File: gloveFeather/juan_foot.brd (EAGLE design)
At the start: 44.4 x 59.4 mm, 8 parts

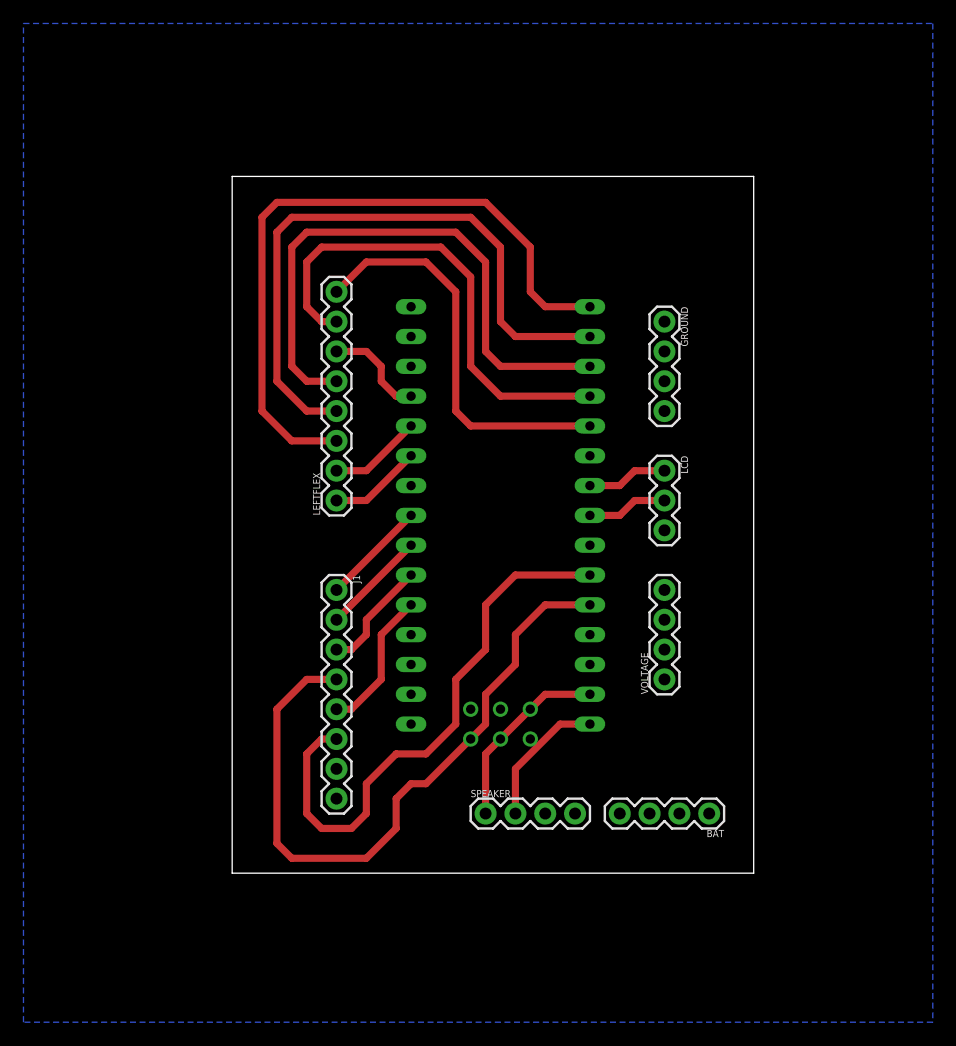
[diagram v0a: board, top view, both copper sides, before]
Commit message: pcb updated with new connections. Added 3V plane
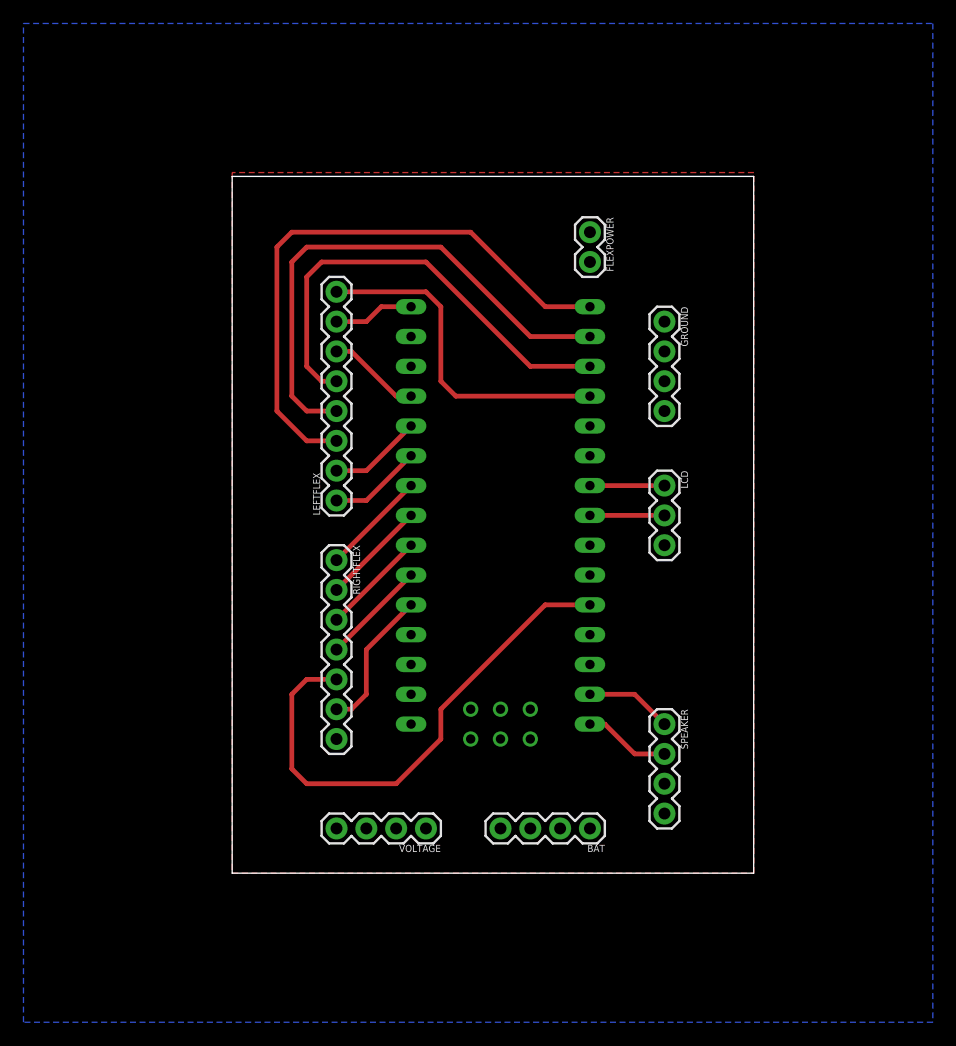
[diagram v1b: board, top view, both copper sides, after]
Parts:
- removed J1: (no value), SparkFun-Connectors:1X08
- added FLEXPOWER: (no value), SparkFun-Connectors:1X02
- added RIGHTFLEX: (no value), SparkFun-Connectors:1X07
- moved VOLTAGE 24.0 mm to (16.5, 3.81), turned to 180 degrees
- moved SPEAKER 17.0 mm to (36.8, 12.7), turned to 270 degrees
- moved BAT 10.2 mm to (30.5, 3.81)
- moved LCD 1.27 mm to (36.8, 33.0)
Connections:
- removed net G: GROUND.1, GROUND.2, GROUND.3, GROUND.4
- removed net N$6: U$1.D7
- new net NA: RIGHTFLEX.7
- net 3V: now also FLEXPOWER.1; no longer J1.8
- net GND: now also FLEXPOWER.2, GROUND.1, GROUND.2, GROUND.3, GROUND.4; no longer J1.7
- net INDEXSIDE: now also RIGHTFLEX.1, U$1.A3; no longer LEFTFLEX.4, U$1.D11
- net MIDDLEB: now also LEFTFLEX.5, U$1.D10; no longer LEFTFLEX.8, U$1.D8
- net MIDDLESIDE: now also LEFTFLEX.4, U$1.D11; no longer LEFTFLEX.7, U$1.D9
- net MIDDLETIP: now also LEFTFLEX.7, U$1.D13; no longer LEFTFLEX.5, U$1.D10
- net PINKYFLEX: now also RIGHTFLEX.6; no longer J1.5
- net PINKYSIDE: now also RIGHTFLEX.5, U$1.D2; no longer J1.6, U$1.D3
- net RINGFLEX: now also RIGHTFLEX.4; no longer J1.3
- net RINGSIDE: now also LEFTFLEX.8, U$1.D9; no longer J1.4, U$1.D2
- net SCL: now also RIGHTFLEX.3; no longer J1.2
- net SDA: now also RIGHTFLEX.2; no longer J1.1
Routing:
- net INDEXSIDE: track 54.0 -> 8.98 mm
- net MIDDLETIP: track 49.6 -> 6.88 mm
- net RINGSIDE: track 58.2 -> 29.0 mm
- net SIN: track 16.1 -> 7.40 mm
- net INDEXTIP: track 58.3 -> 49.9 mm
- net MIDDLEB: track 34.4 -> 39.0 mm
- net SOUT: track 11.7 -> 7.40 mm
- net MIDDLESIDE: track 41.3 -> 44.8 mm
- net PINKYSIDE: track 47.7 -> 44.4 mm
- net MIDDLEFLEX: track 8.67 -> 7.93 mm
- net RINGFLEX: track 9.72 -> 8.98 mm
- net STX: track 6.88 -> 6.35 mm
- net SRX: track 6.88 -> 6.35 mm
- added copper zone on layer 1, net 3V

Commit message: finished glove pcb and speaker pcb
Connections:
- removed net N$9: U$1.GND1
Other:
- board size 44.4 x 59.4 mm -> 40.6 x 58.1 mm
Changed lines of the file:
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@@
 <board>
 <plain>
-<wire x1="0" y1="0" x2="44.43" y2="0" width="0" layer="20"/>
-<wire x1="44.43" y1="0" x2="44.43" y2="59.36" width="0" layer="20"/>
-<wire x1="44.43" y1="59.36" x2="0" y2="59.36" width="0" layer="20"/>
-<wire x1="0" y1="59.36" x2="0" y2="0" width="0" layer="20"/>
+<wire x1="1.27" y1="0" x2="41.89" y2="0" width="0" layer="20"/>
+<wire x1="41.89" y1="0" x2="41.89" y2="58.09" width="0" layer="20"/>
+<wire x1="41.89" y1="58.09" x2="1.27" y2="58.09" width="0" layer="20"/>
+<wire x1="1.27" y1="58.09" x2="1.27" y2="0" width="0" layer="20"/>
 </plain>
 <attributes>
@@
 <contactref element="U$1" pad="RAW"/>
 <contactref element="FLEXPOWER" pad="1"/>
-<wire x1="15.24" y1="12.7" x2="30.48" y2="54.61" width="0" layer="19" extent="1-1"/>
-<wire x1="25.4" y1="3.81" x2="15.24" y2="12.7" width="0" layer="19" extent="1-1"/>
-<wire x1="36.83" y1="7.62" x2="25.4" y2="3.81" width="0" layer="19" extent="1-1"/>
 <polygon width="0.4064" layer="1" isolate="0.4064">
-<vertex x="0" y="59.69"/>
-<vertex x="0" y="0"/>
-<vertex x="44.45" y="0"/>
-<vertex x="44.45" y="59.69"/>
+<vertex x="-2.54" y="59.69"/>
+<vertex x="-2.54" y="0"/>
+<vertex x="43.18" y="0"/>
+<vertex x="43.18" y="59.69"/>
 </polygon>
 </signal>
@@
 <wire x1="8.89" y1="3.81" x2="11.43" y2="3.81" width="0" layer="19" extent="1-1"/>
 </signal>
-<signal name="N$9">
-<contactref element="U$1" pad="GND1"/>
-</signal>
 <signal name="SRX">

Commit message: final pcb
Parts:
- removed GROUND, VOLTAGE: (no value), SparkFun-Connectors:1X04
- removed U$1: NANO, Arduino-clone:NANO
- added J1: (no value), SparkFun-Connectors:1X01
- added LEFTFEATHER, RIGHTFEATHER: (no value), SparkFun-Connectors:1X15
- moved FLEXPOWER 50.5 mm to (31.8, 4.08), turned to 0 degrees
- moved BAT 7.62 mm to (22.9, 4.08)
- moved LCD 4.02 mm to (40.6, 31.8)
- moved SPEAKER 3.81 mm to (40.6, 12.7)
- moved LEFTFLEX 2.84 mm to (11.4, 30.5)
- moved RIGHTFLEX 1.27 mm to (8.89, 25.4)
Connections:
- removed net V: VOLTAGE.1, VOLTAGE.2, VOLTAGE.3, VOLTAGE.4
- new net 5V: LEFTFEATHER.4
- new net D3: RIGHTFEATHER.6
- new net D4: RIGHTFEATHER.7
- new net D7: RIGHTFEATHER.10
- new net N$13: LEFTFEATHER.13
- new net RST: LEFTFEATHER.3, RIGHTFEATHER.3
- new net VIN: BAT.3, LEFTFEATHER.1
- net 3V: now also J1.1, LEFTFEATHER.14; no longer BAT.3, U$1.RAW
- net GND: now also LEFTFEATHER.2, RIGHTFEATHER.4; no longer GROUND.1, GROUND.2, GROUND.3, GROUND.4, U$1.GND
- net INDEXFLEX: now also LEFTFEATHER.11; no longer U$1.A1
- net INDEXSIDE: now also LEFTFEATHER.9; no longer U$1.A3
- net INDEXTIP: now also RIGHTFEATHER.14; no longer U$1.D12
- net MIDDLEB: now also RIGHTFEATHER.12; no longer U$1.D10
- net MIDDLEFLEX: now also LEFTFEATHER.12; no longer U$1.A0
- net MIDDLESIDE: now also RIGHTFEATHER.13; no longer U$1.D11
- net MIDDLETIP: now also LEFTFEATHER.15; no longer U$1.D13
- net PINKYFLEX: now also LEFTFEATHER.5; no longer U$1.A7
- net PINKYSIDE: now also RIGHTFEATHER.15; no longer U$1.D2
- net RINGFLEX: now also LEFTFEATHER.6; no longer U$1.A6
- net RINGSIDE: now also RIGHTFEATHER.11; no longer U$1.D9
- net SCL: now also LEFTFEATHER.7; no longer U$1.A5
- net SDA: now also LEFTFEATHER.8; no longer U$1.A4
- net SIN: now also RIGHTFEATHER.2; no longer U$1.RX1
- net SOUT: now also RIGHTFEATHER.1; no longer U$1.TX0
- net SRX: now also RIGHTFEATHER.9; no longer U$1.D6
- net STX: now also RIGHTFEATHER.8; no longer U$1.D5
- net THUMBFLEX: now also LEFTFEATHER.10; no longer U$1.A2
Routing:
- net 3V: track 0.00 -> 85.3 mm
- net GND: track 0.00 -> 70.1 mm
- net PINKYSIDE: track 44.4 -> 80.8 mm
- net PINKYFLEX: track 12.3 -> 35.6 mm
- net SDA: track 8.98 -> 28.1 mm
- net SCL: track 8.98 -> 28.1 mm
- net RINGFLEX: track 8.98 -> 28.1 mm
- net VIN: track 0.00 -> 18.3 mm
- net MIDDLEFLEX: track 7.93 -> 20.9 mm
- net THUMBFLEX: track 7.93 -> 20.3 mm
- net INDEXFLEX: track 7.93 -> 20.3 mm
- net MIDDLETIP: track 6.88 -> 18.8 mm
- net INDEXTIP: track 49.9 -> 59.5 mm
- net MIDDLESIDE: track 44.8 -> 52.5 mm
- net MIDDLEB: track 39.0 -> 45.6 mm
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- added copper zone on layer 16, net 3V
- removed copper zone on layer 1, net 3V
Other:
- board size 40.6 x 58.1 mm -> 47 x 57.4 mm
